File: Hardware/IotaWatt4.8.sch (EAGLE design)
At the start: 53 parts

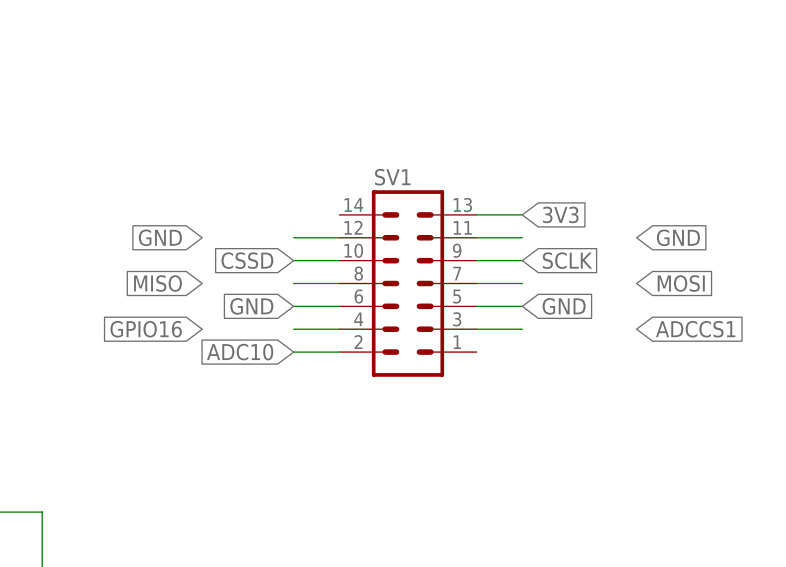
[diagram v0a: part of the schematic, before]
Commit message: completed routing for both boards
routed out both the base and IO board. Should be ready for verification
There will be errors.
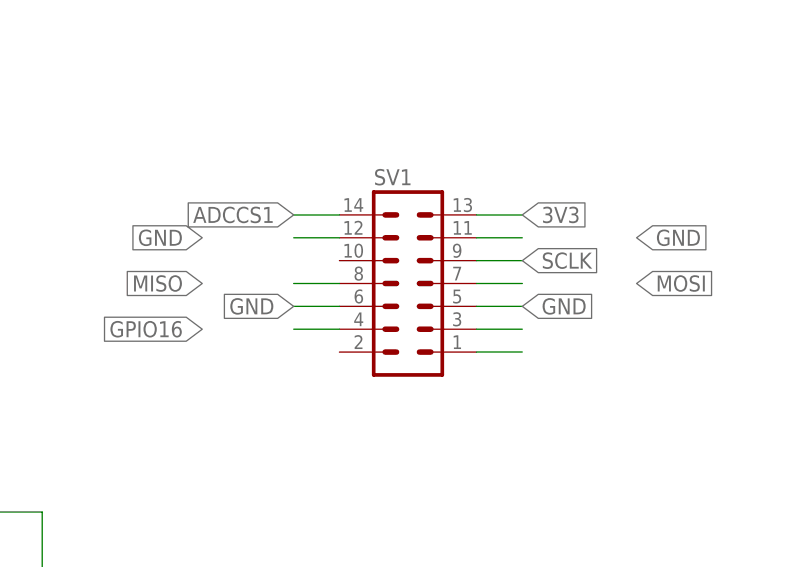
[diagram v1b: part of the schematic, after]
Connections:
- removed net CSSD: SV1.10
- net 5V: now also SV1.3
- net ADC10: no longer SV1.2
- net ADCCS0: now also SV1.1
- net ADCCS1: now also SV1.14; no longer SV1.3
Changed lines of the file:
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@@
 </segment>
 <segment>
-<pinref part="SV1" gate="G$1" pin="3"/>
-<wire x1="243.84" y1="15.24" x2="248.92" y2="15.24" width="0.1524" layer="91"/>
-<label x="261.62" y="15.24" size="1.778" layer="91" font="vector" xref="yes"/>
+<pinref part="SV1" gate="G$1" pin="14"/>
+<wire x1="228.6" y1="27.94" x2="223.52" y2="27.94" width="0.1524" layer="91"/>
+<label x="223.52" y="27.94" size="1.778" layer="91" rot="R180" xref="yes"/>
 </segment>
 </net>
@@
 <label x="55.88" y="-104.14" size="1.778" layer="91" xref="yes"/>
 </segment>
-</net>
-<net name="CSSD" class="0">
-<segment>
-<pinref part="SV1" gate="G$1" pin="10"/>
-<wire x1="228.6" y1="22.86" x2="223.52" y2="22.86" width="0.1524" layer="91"/>
-<label x="223.52" y="22.86" size="1.778" layer="91" font="vector" rot="R180" xref="yes"/>
+<segment>
+<pinref part="SV1" gate="G$1" pin="1"/>
+<wire x1="243.84" y1="12.7" x2="248.92" y2="12.7" width="0.1524" layer="91"/>
 </segment>
 </net>
@@
 <pinref part="U$20" gate="G$1" pin="6"/>
 <wire x1="88.9" y1="-76.2" x2="81.28" y2="-76.2" width="0.25" layer="91"/>
-</segment>
-<segment>
-<pinref part="SV1" gate="G$1" pin="2"/>
-<wire x1="228.6" y1="12.7" x2="223.52" y2="12.7" width="0.1524" layer="91"/>
-<label x="223.52" y="12.7" size="1.778" layer="91" font="vector" rot="R180" xref="yes"/>
 </segment>
 <segment>
@@
 <label x="93.98" y="119.38" size="1.778" layer="95" xref="yes"/>
 </segment>
-</net>
+<segment>
+<pinref part="SV1" gate="G$1" pin="3"/>
+<wire x1="243.84" y1="15.24" x2="248.92" y2="15.24" width="0.1524" layer="91"/>
+</segment>
+</net>

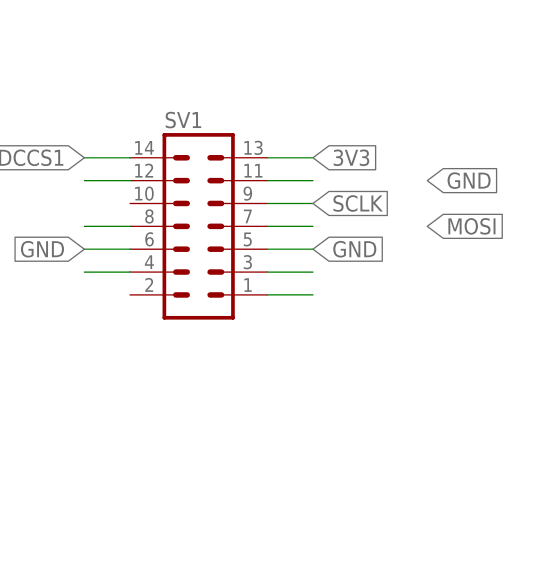
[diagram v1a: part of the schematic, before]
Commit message: added mechcad files
case and transformer files
case source:
https://eng.italtronic.com/products/modulbox_one_en/4m_modulbox_one_en/
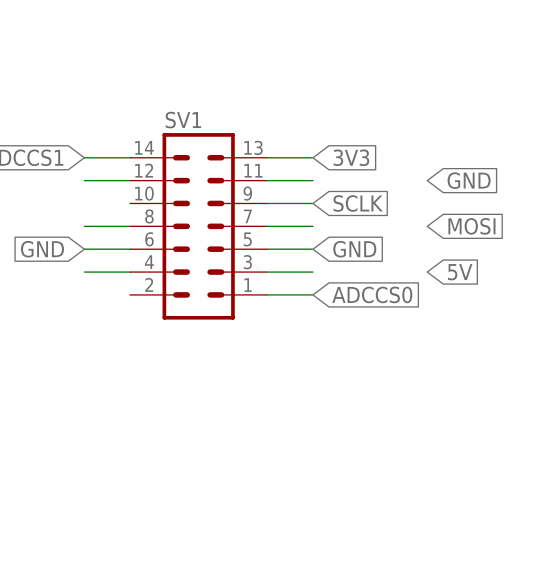
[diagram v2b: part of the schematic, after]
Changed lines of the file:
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@@
 <pinref part="SV1" gate="G$1" pin="1"/>
 <wire x1="243.84" y1="12.7" x2="248.92" y2="12.7" width="0.1524" layer="91"/>
+<label x="248.92" y="12.7" size="1.778" layer="91" xref="yes"/>
 </segment>
 </net>
@@
 <pinref part="SV1" gate="G$1" pin="3"/>
 <wire x1="243.84" y1="15.24" x2="248.92" y2="15.24" width="0.1524" layer="91"/>
-</segment>
-</net>
+<label x="261.62" y="15.24" size="1.778" layer="91" xref="yes"/>
+</segment>
+</net>

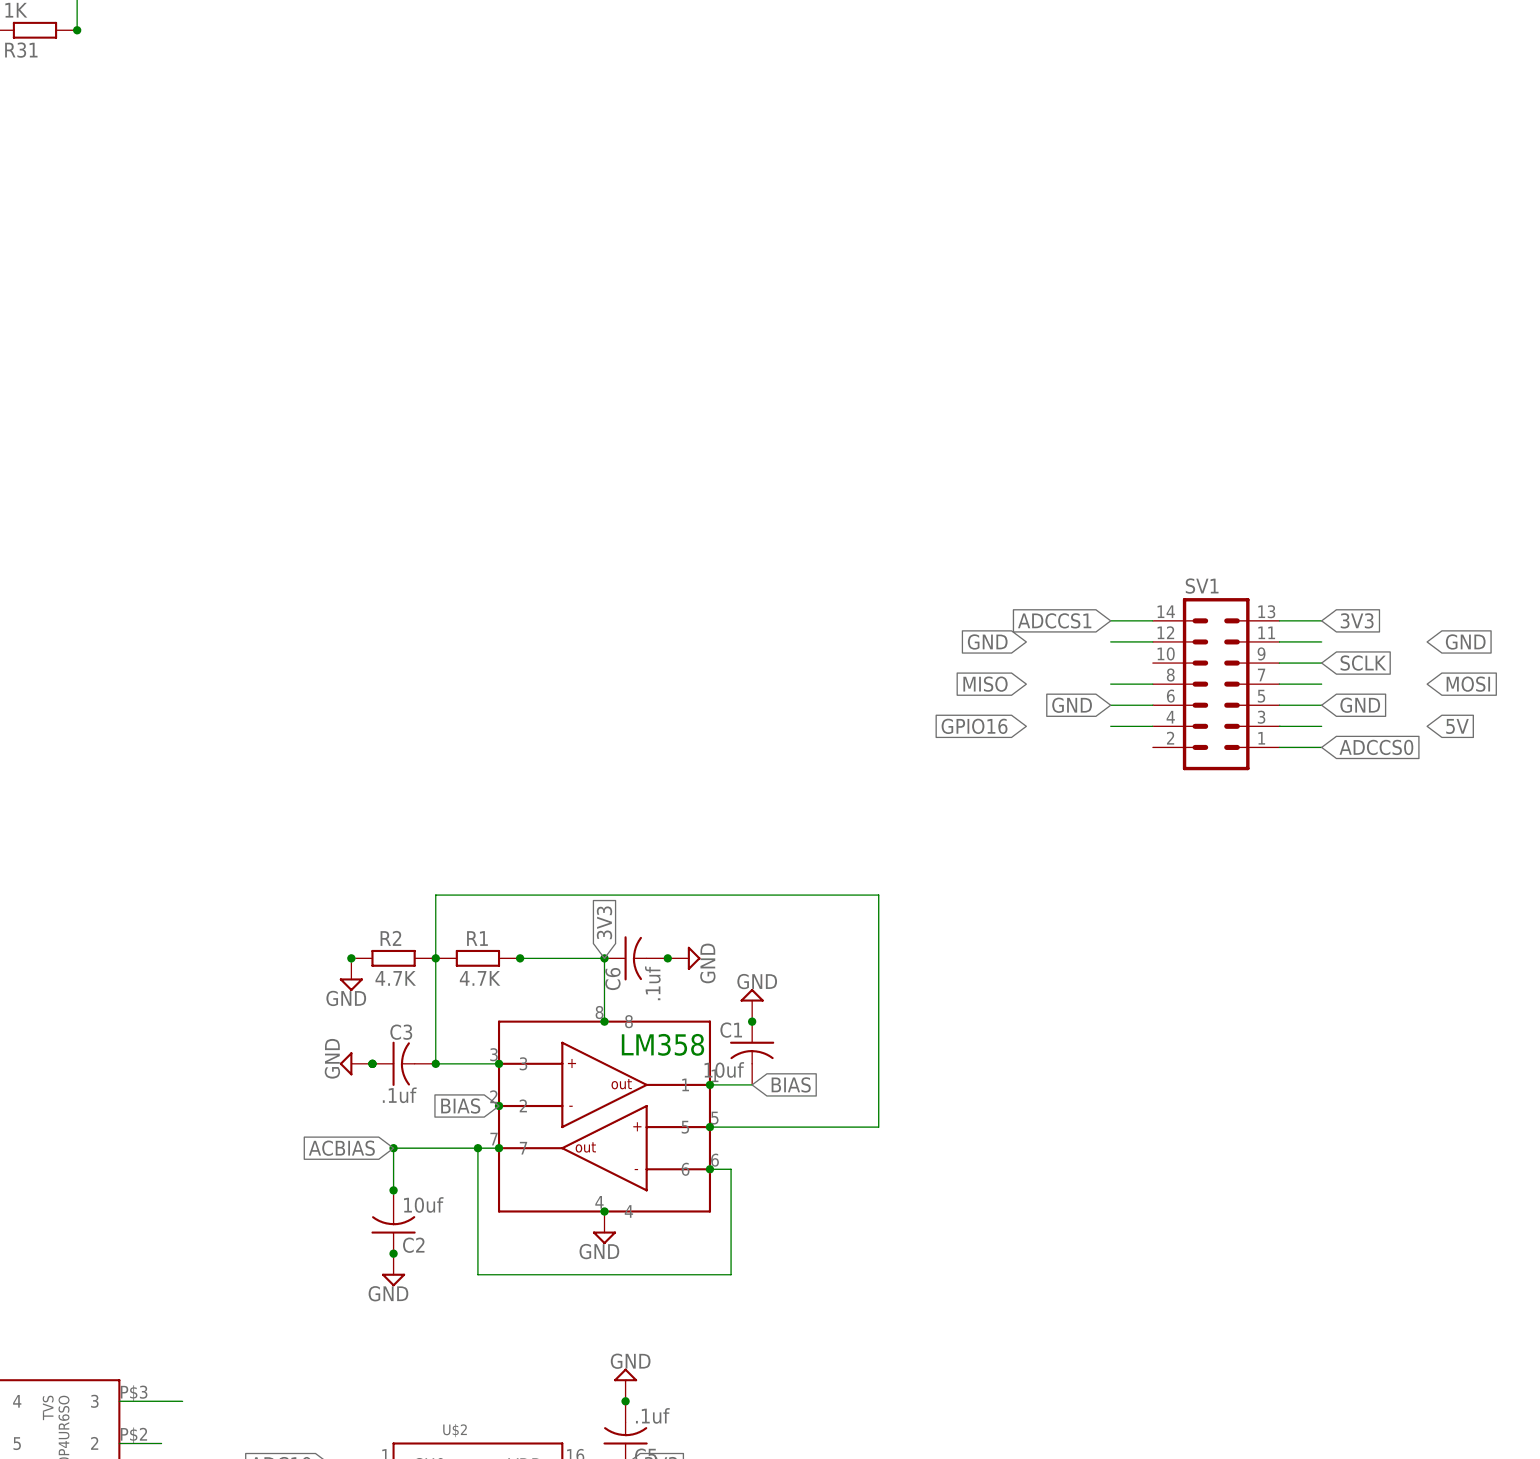
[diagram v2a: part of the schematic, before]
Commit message: beginning to add a 2.2" TFT display
not quite sure about the mechanical layout yet.
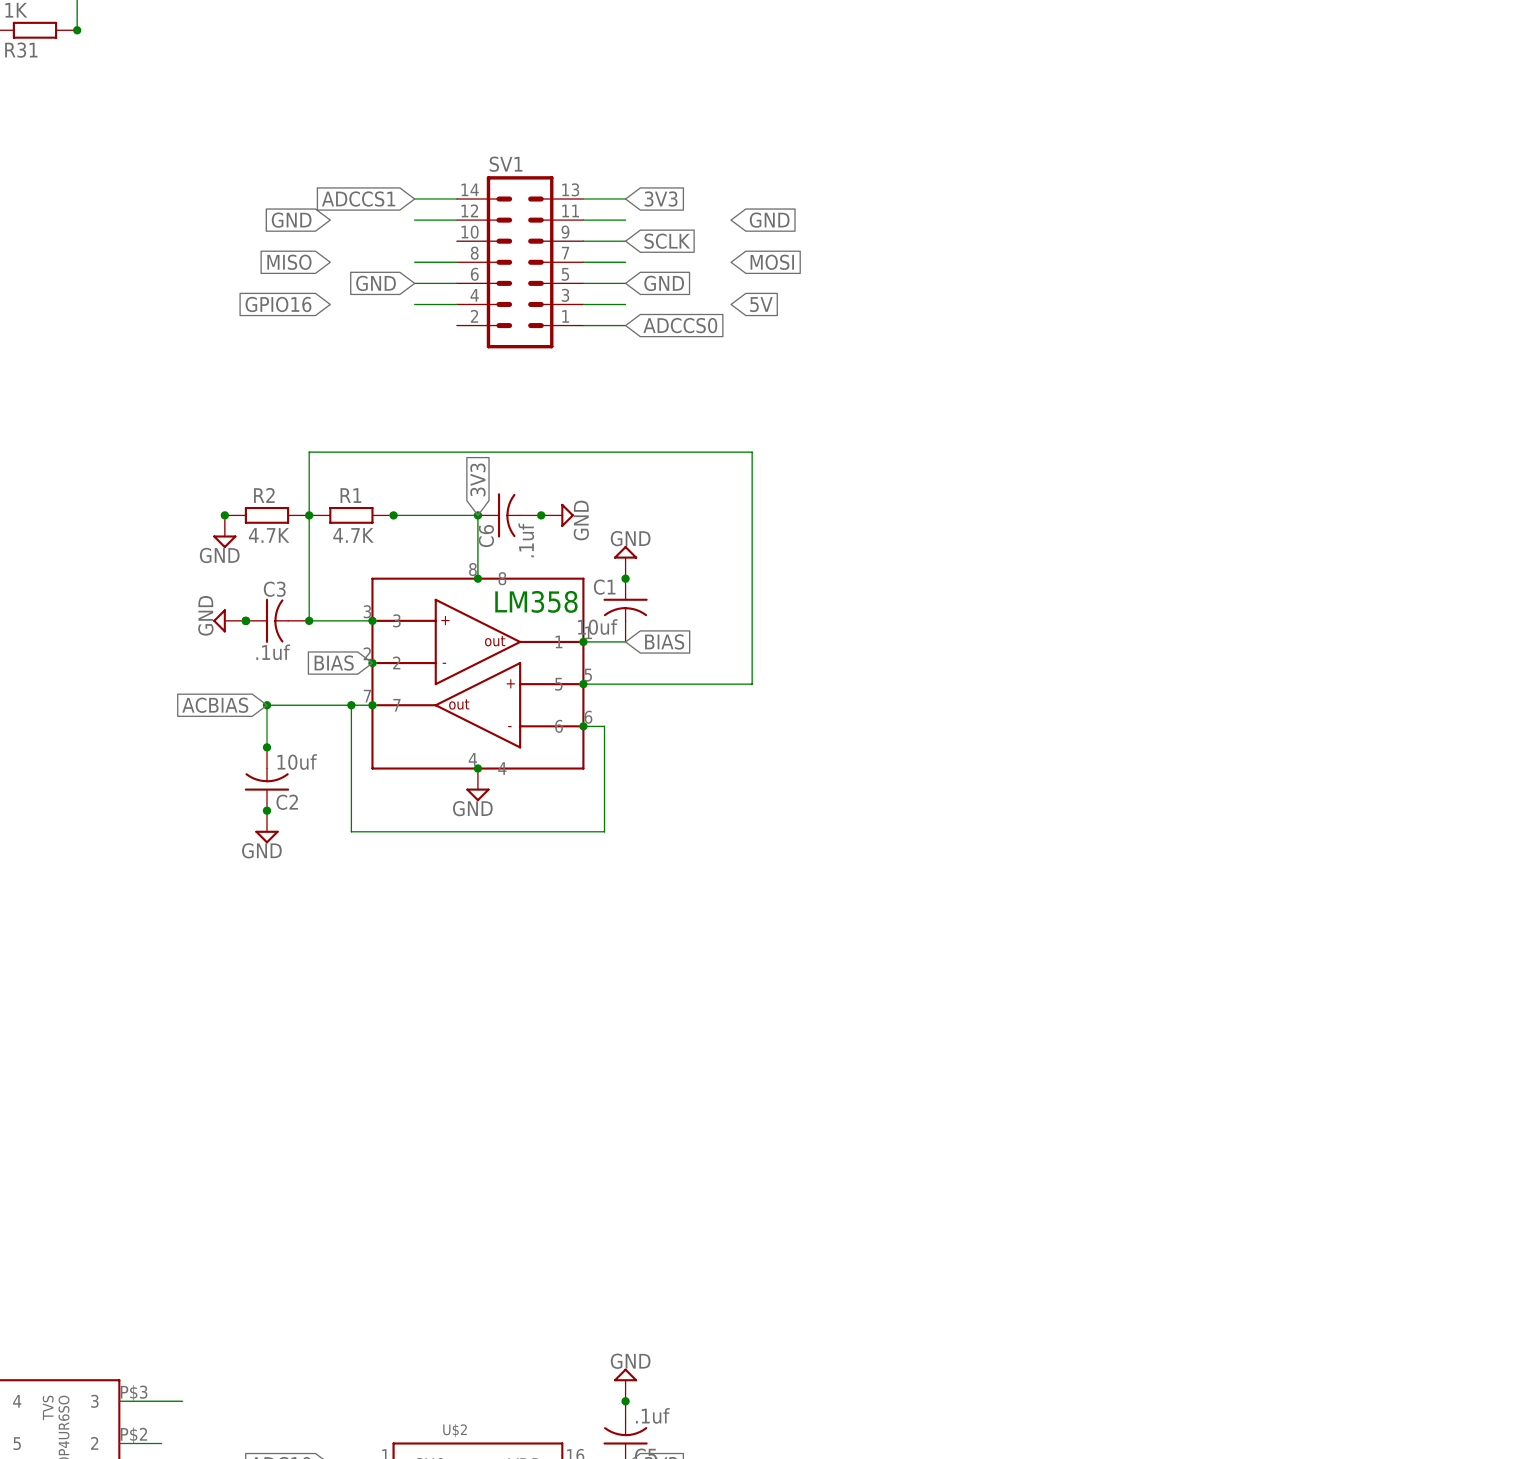
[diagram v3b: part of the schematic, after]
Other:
- moved on the sheet: C1, C2, C3, C6, R1, R2, SV1

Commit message: Revert "beginning to add a 2.2" TFT display"
This reverts commit 5a3055f75d7c66bfc0e3a1cc9d4d5180e17e1807.
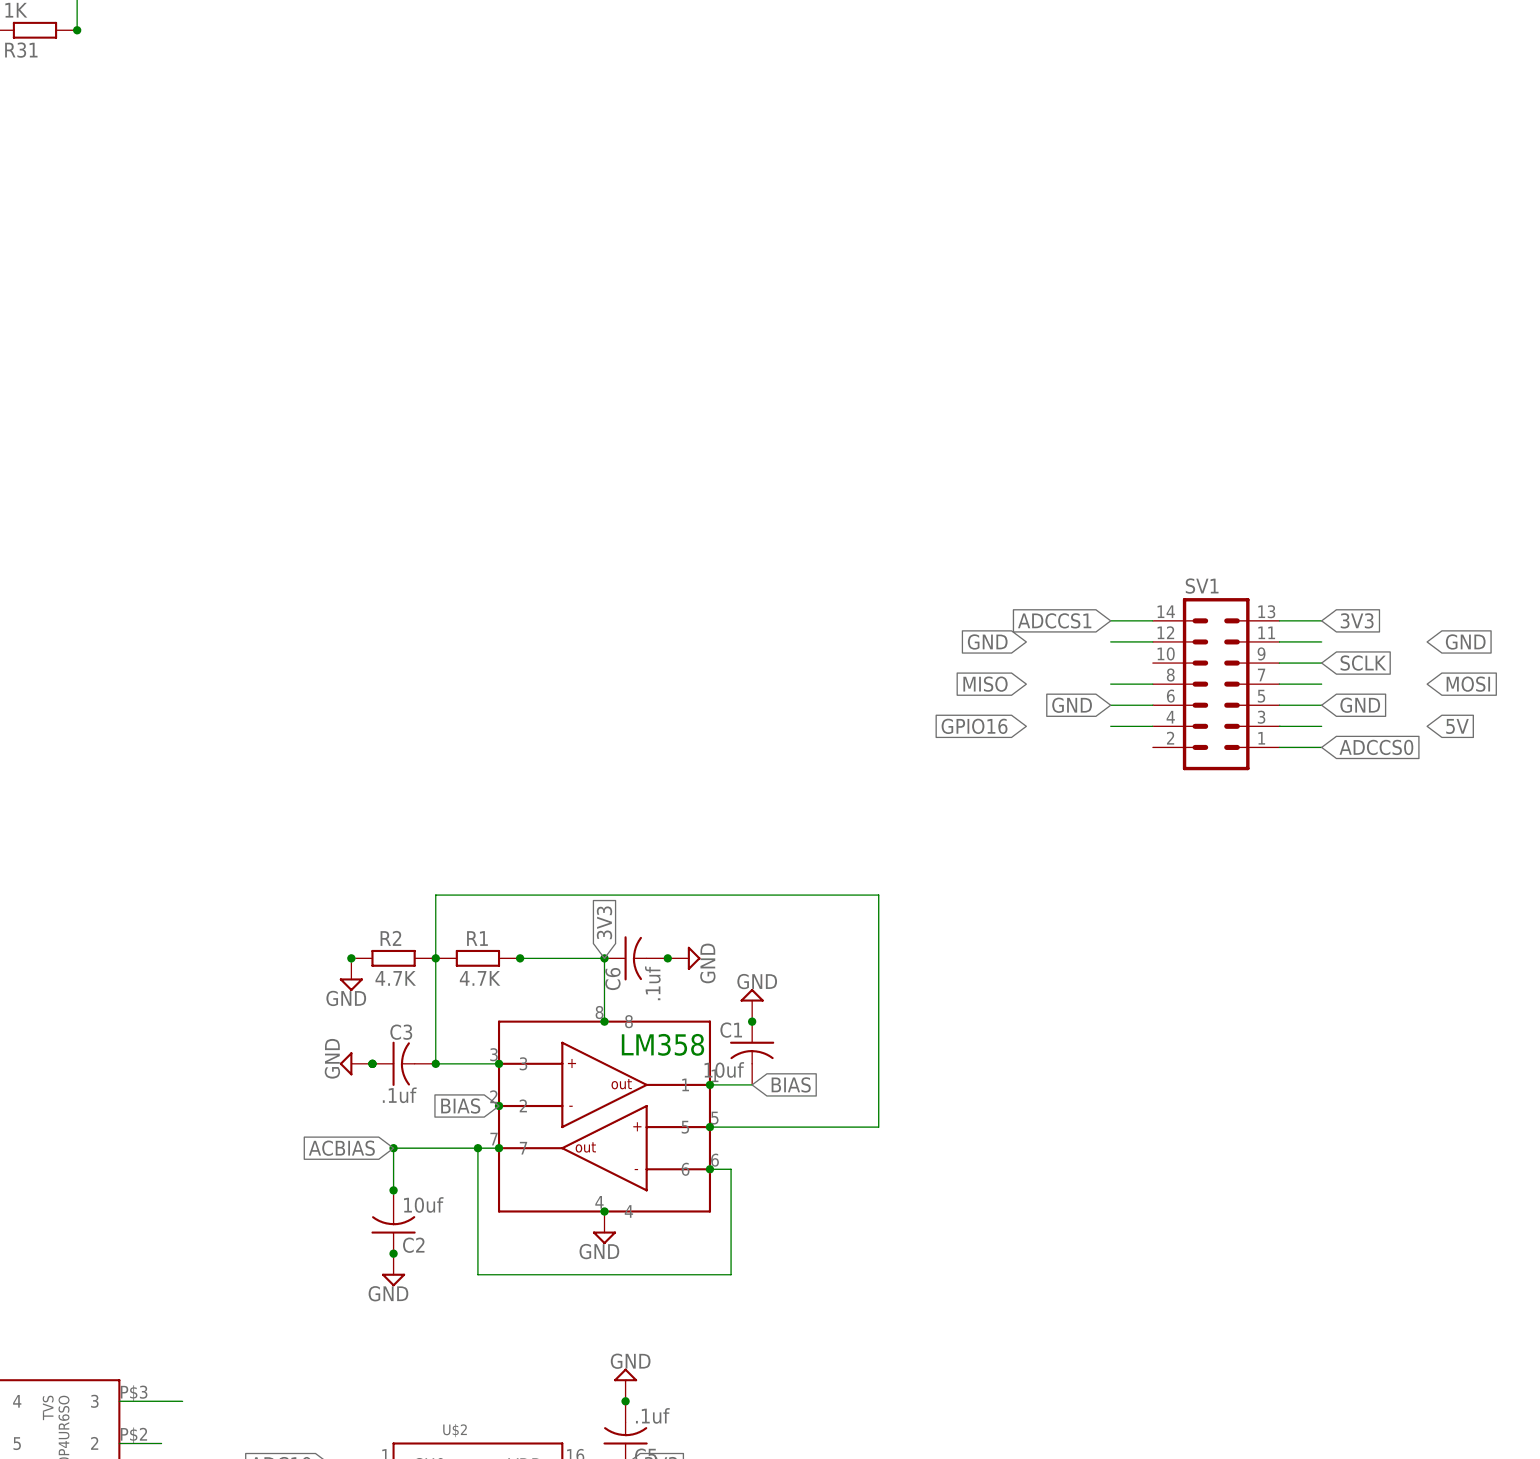
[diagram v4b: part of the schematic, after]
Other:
- moved on the sheet: C1, C2, C3, C6, R1, R2, SV1
